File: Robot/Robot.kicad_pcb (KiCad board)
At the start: 2 copper layers, 100 x 100 mm, 31 parts, among them J1 Barrel_Jack, J10 Conn_01x03_Pin, J11 Stepper_2, J2 Conn_01x02_Pin, J3 Stepper_2, J4 UltraSonic, J5 MotorController, J6 Range, J7 Conn_01x04_Pin, J8 Conn_01x03_Pin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

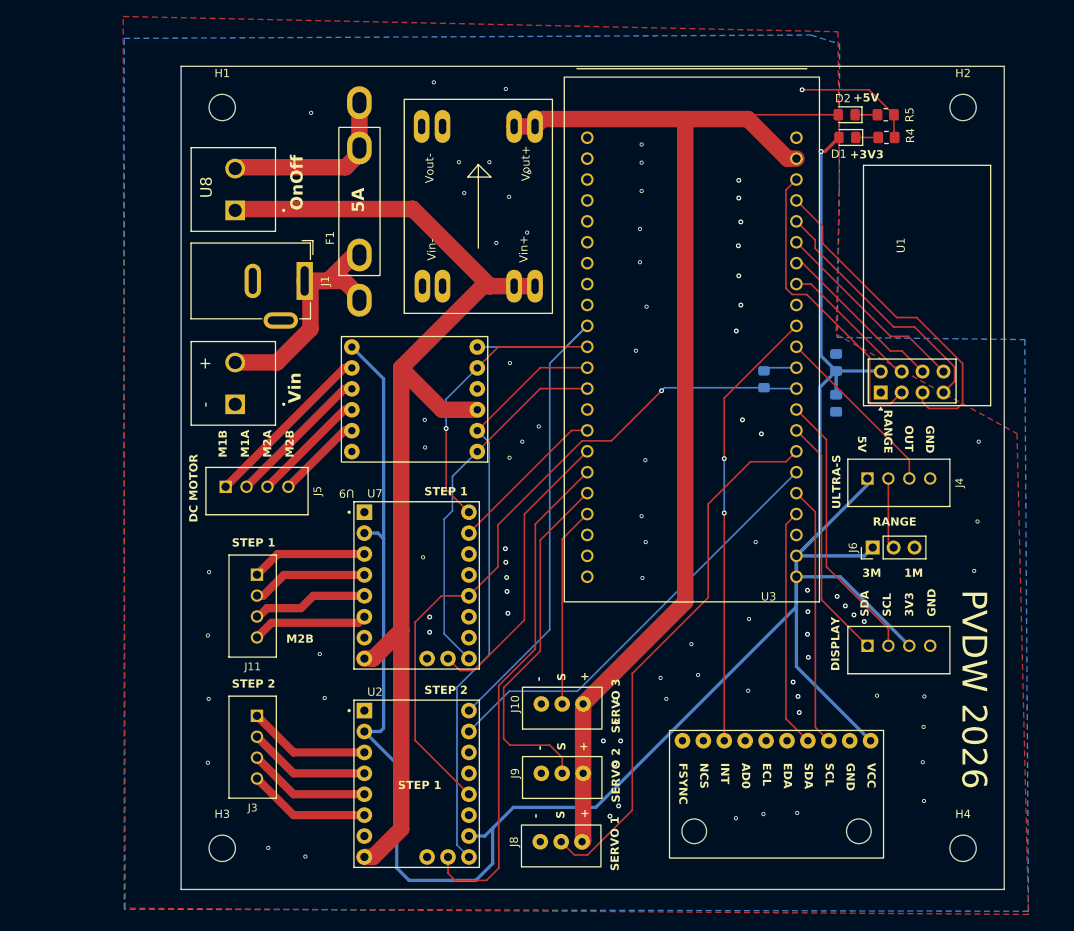
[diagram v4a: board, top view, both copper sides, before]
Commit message: New PCB Layout for Robot
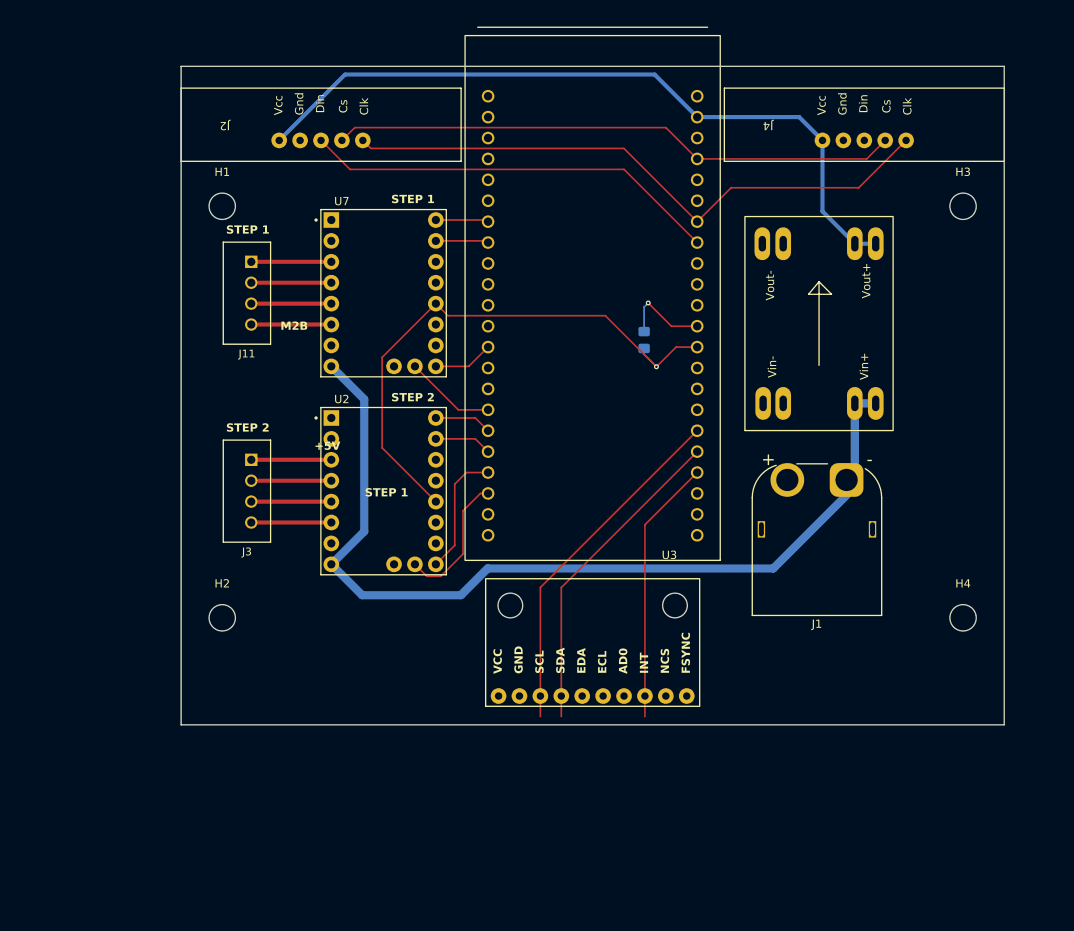
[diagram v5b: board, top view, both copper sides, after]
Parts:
- removed C1: 4u7, Capacitor_SMD:C_0805_2012Metric_Pad1.18x1.45mm_HandSolder
- removed C2: 100N, Capacitor_SMD:C_0805_2012Metric_Pad1.18x1.45mm_HandSolder
- removed D1: LED_GREEN, LED_SMD:LED_0805_2012Metric_Pad1.15x1.40mm_HandSolder
- removed D2: LED_RED, LED_SMD:LED_0805_2012Metric_Pad1.15x1.40mm_HandSolder
- removed F1: Fuse, PVDW_custom:FUSE_3544-2
- removed J10, J8, J9: Conn_01x03_Pin, PVDW_custom:3PIN_SERVO
- removed J5: MotorController, PVDW_custom:Connector_1x4_p2.54_vertical_stepper
- removed J6: Range, Connector_PinHeader_2.54mm:PinHeader_1x03_P2.54mm_Vertical
- removed J7: Conn_01x04_Pin, PVDW_custom:Connector_1x4_p2.54_vertical_stepper
- removed R4, R5: 1k2, Resistor_SMD:R_0805_2012Metric_Pad1.20x1.40mm_HandSolder
- removed U1: NRF24L01_Breakout, PVDW_custom:nRF24L01_Breakout
- removed U8: On_Off, PVDW_custom:screw_block_2pin
- removed U9: ~, PVDW_custom:DRV8833
- J1: value Barrel_Jack -> Conn_01x02_Pin; footprint PVDW_custom:DC_Jack_PCB -> Connector_AMASS:AMASS_XT60PW-M_1x02_P7.20mm_Horizontal
- J2: value Conn_01x02_Pin -> Dsp1; footprint PVDW_custom:screw_block_2pin -> PVDW_custom:PinHeader_max7219
- J4: value UltraSonic -> Dsp2; footprint PVDW_custom:Connector_1x4_p2.54_vertical_stepper -> PVDW_custom:PinHeader_max7219
- moved H3 119.1 mm to (195.0, 67.0)
- moved H2 109.3 mm to (105.0, 117.0)
- moved J1 70.1 mm to (180.8, 100.2), turned to 180 degrees
- moved U4 43.8 mm to (177.5, 81.2)
- moved J4 41.8 mm to (183.0, 59.0), turned to 90 degrees
- moved J11 38.0 mm to (108.0, 77.6)
- moved U2 35.8 mm to (124.6, 101.6)
- moved U7 35.7 mm to (124.6, 77.6)
- moved J2 33.7 mm to (117.0, 59.0)
- moved J3 31.1 mm to (108.0, 101.6)
- moved U5 29.0 mm to (150.0, 120.0), turned to 90 degrees
- moved H4 28.0 mm to (195.0, 117.0)
- moved R1 15.3 mm to (156.2, 83.2)
- moved U3 13.1 mm to (150.0, 77.0)
- moved H1 12.0 mm to (105.0, 67.0)
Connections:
- net /MC_IN1_S1_EN renamed /S1_EN
- J1 pad 1: VBat -> VDC
- J2 pad 1: GND -> +5V
- J2 pad 2: VBat -> GND
- J4 pad 1: +3.3V -> +5V
- J4 pad 2: Net-(J4-Pin_2) -> GND
- J4 pad 3: /US_OUT -> unconnected-(J4-Pin_3-Pad3)
- J4 pad 4: GND -> /CS
- U2 pad 16: /MC_IN2_S2_EN -> /S2_EN
- U2 pad 9: /MC_IN4_S2_DIR -> /S2_DIR
- U3 pad J1_13: /IMU_INT -> unconnected-(U3-GPIO3-PadJ1_13)
- U3 pad J1_15: /NRF_CSN -> /MOSI
- U3 pad J1_16: /NRF_MOSI -> /CLK
- U3 pad J1_17: /NRF_IRQ -> unconnected-(U3-GPIO11-PadJ1_17)
- U3 pad J1_18: /NRF_MISO -> unconnected-(U3-GPIO12-PadJ1_18)
- U3 pad J1_19: /NRF_CLK -> /CS
- U3 pad J1_20: /NRF_CE -> unconnected-(U3-GPIO14-PadJ1_20)
- U3 pad J1_4: /IMU_SDA -> /IMU_INT
- U3 pad J1_5: /IMU_SCL -> /IMU_SDA
- U3 pad J1_6: /S2_STEP -> /IMU_SCL
- U3 pad J1_7: /SIG_SERVO_1 -> unconnected-(U3-GPIO7-PadJ1_7)
- U3 pad J1_8: /DSP_SDA -> unconnected-(U3-GPIO15-PadJ1_8)
- U3 pad J1_9: /DSP_SCL -> unconnected-(U3-GPIO16-PadJ1_9)
- U3 pad J3_11: /MC_IN2_S2_EN -> unconnected-(U3-GPIO37-PadJ3_11)
- U3 pad J3_12: /MC_IN3_S1_DIR -> unconnected-(U3-GPIO36-PadJ3_12)
- U3 pad J3_13: /MC_IN4_S2_DIR -> unconnected-(U3-GPIO35-PadJ3_13)
- U3 pad J3_15: unconnected-(U3-GPIO45-PadJ3_15) -> /S1_STEP
- U3 pad J3_16: unconnected-(U3-GPIO48-PadJ3_16) -> /S1_DIR
- U3 pad J3_3: unconnected-(U3-U0RXD/GPIO44-PadJ3_3) -> /S2_DIAG
- U3 pad J3_4: /SIG_SERVO_3 -> /S2_EN
- U3 pad J3_5: /SIG_SERVO_2 -> /S2_STEP
- U3 pad J3_6: /S2_DIAG -> /S2_DIR
- U3 pad J3_8: /S1_STEP -> unconnected-(U3-MTDO/GPIO40-PadJ3_8)
- U7 pad 9: /MC_IN3_S1_DIR -> /S1_DIR
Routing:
- net +3.3V: track 275.3 -> 0.00 mm, vias 1 -> 0
- net /CLK: track 0.00 -> 74.2 mm
- net /MC_IN2_S2_EN: track 71.1 -> 0.00 mm
- net /CS: track 0.00 -> 69.2 mm
- net /MC_IN4_S2_DIR: track 67.1 -> 0.00 mm
- net /SIG_SERVO_1: track 65.9 -> 0.00 mm
- net +5V: track 140.8 -> 89.3 mm
- net /MOSI: track 0.00 -> 50.8 mm
- net /S2_STEP: track 52.8 -> 6.99 mm
- net /S2_DIAG: track 61.7 -> 16.7 mm
- net /SIG_SERVO_2: track 44.0 -> 0.00 mm
- net /NRF_CLK: track 41.0 -> 0.00 mm
- net /NRF_CE: track 37.5 -> 0.00 mm
- net /S1_EN: track 44.6 -> 7.31 mm
- net /MC_IN3_S1_DIR: track 34.7 -> 0.00 mm, vias 1 -> 0
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- removed copper zone on B.Cu, net GND
- removed copper zone on F.Cu, net GND
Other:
- board size 100 x 100 mm -> 100 x 80 mm
- board text removed: "+"
- board text removed: "+3V3"
- board text removed: "-"
- board text removed: "1M"
- board text removed: "3M"
- board text removed: "5A"
- board text removed: "OnOff"
- board text removed: "PVDW 2026"
- board text removed: "RANGE"
- board text removed: "SDA"
- board text removed: "Vin"

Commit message: New version
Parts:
- removed U4: ~, PVDW_custom:LM1584EN
- added C1: C_Polarized, Capacitor_THT:C_Radial_D10.0mm_H20.0mm_P5.00mm, F.Cu at (157.0, 91.0)
- added C2: C_Polarized, Capacitor_THT:C_Radial_D10.0mm_H20.0mm_P5.00mm, F.Cu at (143.0, 91.0)
- added U1: LM7805_TO220, Package_TO_SOT_THT:TO-220-3_Vertical, F.Cu at (147.5, 103.5)
- J1: footprint Connector_AMASS:AMASS_XT60PW-M_1x02_P7.20mm_Horizontal -> Connector_AMASS:AMASS_XT60-F_1x02_P7.20mm_Vertical
- J2: footprint PVDW_custom:PinHeader_max7219 -> Connector_PinHeader_2.54mm:PinHeader_1x05_P2.54mm_Vertical
- J4: value Dsp2 -> Conn_01x02_Pin; footprint PVDW_custom:PinHeader_max7219 -> Connector_PinHeader_2.54mm:PinHeader_1x02_P2.54mm_Vertical
- moved J1 60.3 mm to (121.0, 107.5), turned to 0 degrees
- moved U5 45.0 mm to (150.0, 75.0)
- moved J4 33.0 mm to (150.0, 60.8), turned to -90 degrees
- moved U3 32.7 mm to (182.3, 82.0)
- moved R1 32.1 mm to (188.0, 87.7)
- moved J2 27.3 mm to (143.8, 54.0)
- moved H1 13.0 mm to (110.0, 55.0)
- moved H3 12.8 mm to (185.0, 75.0)
- moved H4 12.2 mm to (185.0, 110.0)
- moved J3 11.8 mm to (110.0, 90.0)
- moved U2 11.6 mm to (125.0, 90.0)
- moved J11 10.7 mm to (110.0, 67.0)
- moved U7 10.6 mm to (125.0, 67.0)
- moved H2 8.60 mm to (110.0, 110.0)
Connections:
- J1 pad 1: VDC -> GND
- J1 pad 2: GND -> VDC
- J4 pad 1: +5V -> /OTA
- U3 pad J1_14: unconnected-(U3-GPIO46-PadJ1_14) -> /OTA
- U3 pad J1_4: /IMU_INT -> unconnected-(U3-GPIO4-PadJ1_4)
- U3 pad J1_5: /IMU_SDA -> unconnected-(U3-GPIO5-PadJ1_5)
- U3 pad J1_6: /IMU_SCL -> unconnected-(U3-GPIO6-PadJ1_6)
- U3 pad J3_12: unconnected-(U3-GPIO36-PadJ3_12) -> /IMU_INT
- U3 pad J3_13: unconnected-(U3-GPIO35-PadJ3_13) -> /IMU_SDA
- U3 pad J3_14: unconnected-(U3-GPIO0-PadJ3_14) -> /IMU_SCL
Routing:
- net +3.3V: track 0.00 -> 132.7 mm, vias 0 -> 4
- net /OTA: track 0.00 -> 52.5 mm
- net /S12_UART: track 68.2 -> 108.2 mm
- net /S2_STEP: track 6.99 -> 45.8 mm
- net /S2_DIR: track 6.99 -> 45.8 mm
- net /S1_DIAG: track 11.1 -> 49.4 mm
- net /S1_STEP: track 6.43 -> 44.8 mm
- net /S1_DIR: track 6.43 -> 44.8 mm
- net /S1_EN: track 7.31 -> 44.5 mm
- net VDC: track 111.4 -> 77.9 mm
- net /S2_DIAG: track 16.7 -> 44.7 mm
- net /S2_EN: track 15.3 -> 41.9 mm
- net /CLK: track 74.2 -> 49.2 mm
- net /CS: track 69.2 -> 50.7 mm
- net /IMU_INT: track 32.3 -> 16.4 mm
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- added copper zone on B.Cu, net +3.3V
- added copper zone on F.Cu, net +3.3V
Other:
- board size 100 x 80 mm -> 100 x 65 mm

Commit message: New version
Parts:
- added J5: Conn_01x05_Pin, Connector_PinHeader_2.54mm:PinHeader_1x05_P2.54mm_Vertical, F.Cu at (150.2, 60.2)
- moved J4 6.02 mm to (144.0, 60.2)
- moved U1 3.25 mm to (147.5, 106.8)
- moved J1 1.55 mm to (121.0, 109.0)
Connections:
- U3 pad J1_12: /US_OUT -> unconnected-(U3-GPIO8-PadJ1_12)
- U3 pad J1_5: unconnected-(U3-GPIO5-PadJ1_5) -> /GPIO5
- U3 pad J1_6: unconnected-(U3-GPIO6-PadJ1_6) -> /GPIO6
- U3 pad J1_7: unconnected-(U3-GPIO7-PadJ1_7) -> /GPIO7
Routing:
- net /GPIO5: track 0.00 -> 77.1 mm
- net /GPIO6: track 0.00 -> 68.6 mm
- net /GPIO7: track 0.00 -> 57.8 mm
- net +5V: track 104.9 -> 151.2 mm
- net +3.3V: track 132.7 -> 176.8 mm
- net /OTA: track 52.5 -> 59.2 mm, vias 0 -> 1
- net VDC: track 77.9 -> 83.7 mm
- net /S2_EN: track 41.9 -> 40.5 mm
- net GND: vias 0 -> 27
- added copper zone on B.Cu, net GND
- added copper zone on F.Cu, net GND
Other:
- board size 100 x 65 mm -> 100 x 67 mm
- board text added: "3V3"
- board text added: "5V"
- board text added: "CLK"
- board text added: "CS"
- board text added: "DTA"
- board text added: "ESP32S3"
- board text added: "GND"
- board text added: "IO5"
- board text added: "IO6"
- board text added: "IO7"
- board text added: "OTA"
- board text added: "PVDW 2026"
- board text added: "VDC 8.4V"
- board text added: "Vin"
- board text added: "Vout"
- board text removed: "+5V"

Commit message: Ordered version
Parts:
- added J6: Conn_01x02_Pin, Connector_PinHeader_2.54mm:PinHeader_1x02_P2.54mm_Vertical, F.Cu at (138.3, 110.3)
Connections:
- J1 pad 2: VDC -> /VBAT
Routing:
- net /VBAT: track 0.00 -> 10.7 mm
- net VDC: track 83.7 -> 78.5 mm
